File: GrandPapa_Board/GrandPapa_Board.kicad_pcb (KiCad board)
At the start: 4 copper layers, 82 x 82 mm, 98 parts, among them J1 3.7V LiPo Single Cell, J11 Dupont 01x04_Male, J2 HARWIN_ROCKET, J3 Dupont_GPS, J4 HARWIN_MINISENSOR, J5 Dupont_Logger, J6 PROG Header, J7 HARWIN_KALMAN, J8 Therm EN Jumper, U1 MCP1642B-50I/MS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

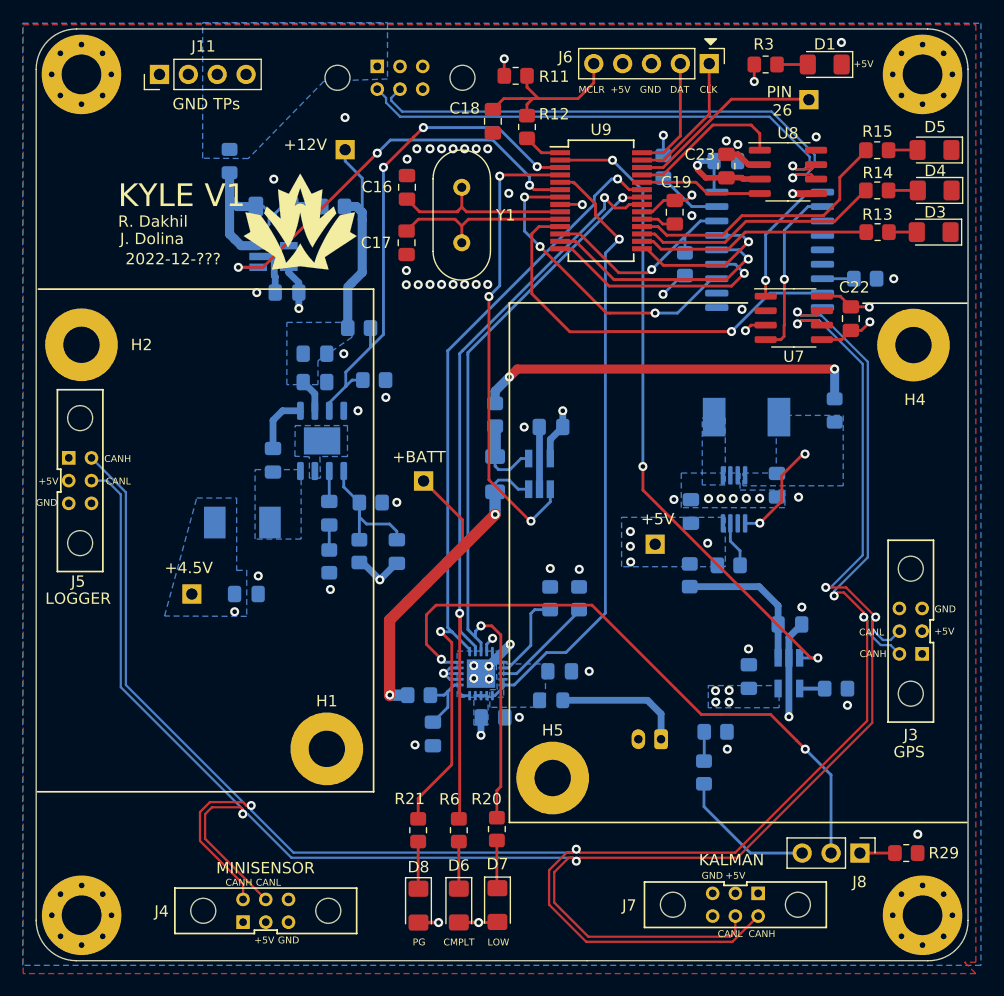
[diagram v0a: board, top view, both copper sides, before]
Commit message: Address Jack's comments, minor schematic text cleanup
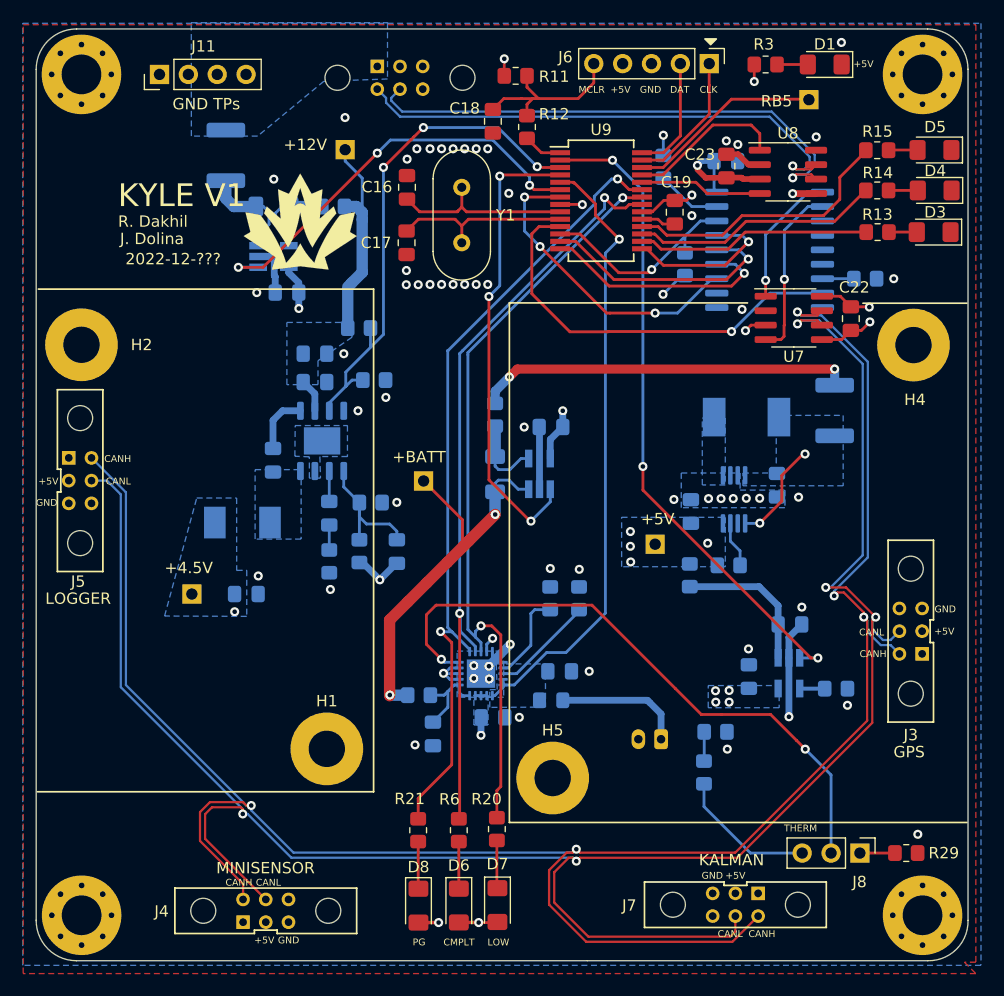
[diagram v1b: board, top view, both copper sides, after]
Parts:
- F1: footprint Fuse:Fuse_0805_2012Metric_Pad1.15x1.40mm_HandSolder -> Fuse:Fuse_1812_4532Metric_Pad1.30x3.40mm_HandSolder
- F2: value 1.2A -> 1.5A; footprint Fuse:Fuse_0805_2012Metric_Pad1.15x1.40mm_HandSolder -> Fuse:Fuse_1812_4532Metric_Pad1.30x3.40mm_HandSolder
- R29: value 15kR -> 10kR
- R4: value 2kR -> 10kR
- moved F1 0.60 mm to (130.0, 71.4)
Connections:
- net /Battery Charging/BATT_CHARGER_PG renamed /Battery Charging/BATT_CHARGER_PG_L
- net /Battery Charging/BATT_CHARGE_COMPLETE renamed /Battery Charging/BATT_CHARGE_COMPLETE_L
- net /Battery Charging/LOW_BAT renamed /Battery Charging/LOW_BAT_L
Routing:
- net Net-(F1-Pad2): track 15.6 -> 9.21 mm
- net +BATT: track 34.4 -> 33.2 mm
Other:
- board text added: "RB5"
- board text added: "THERM"
- board text removed: "PIN 26"

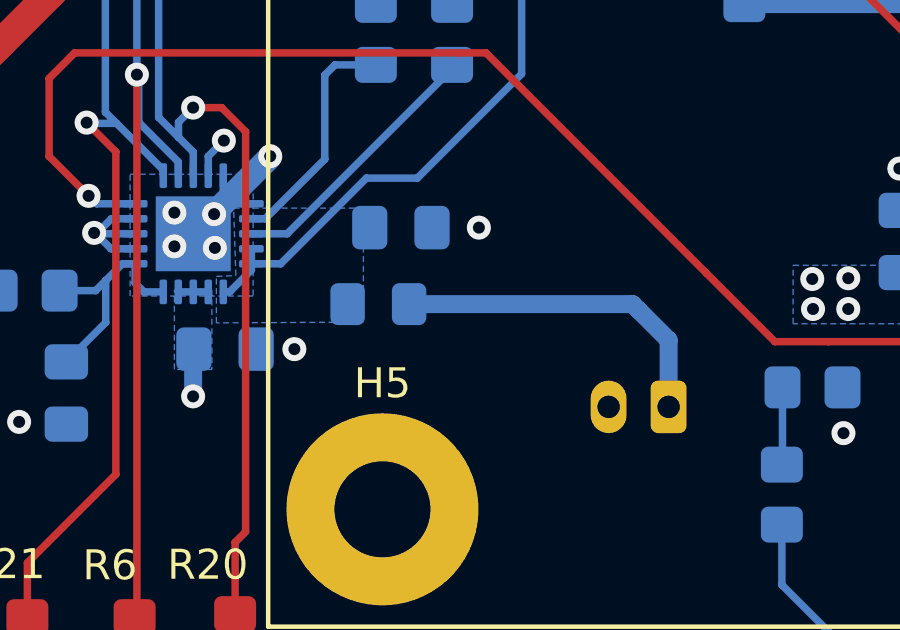
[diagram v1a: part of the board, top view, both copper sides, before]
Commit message: missed F3, update PDF
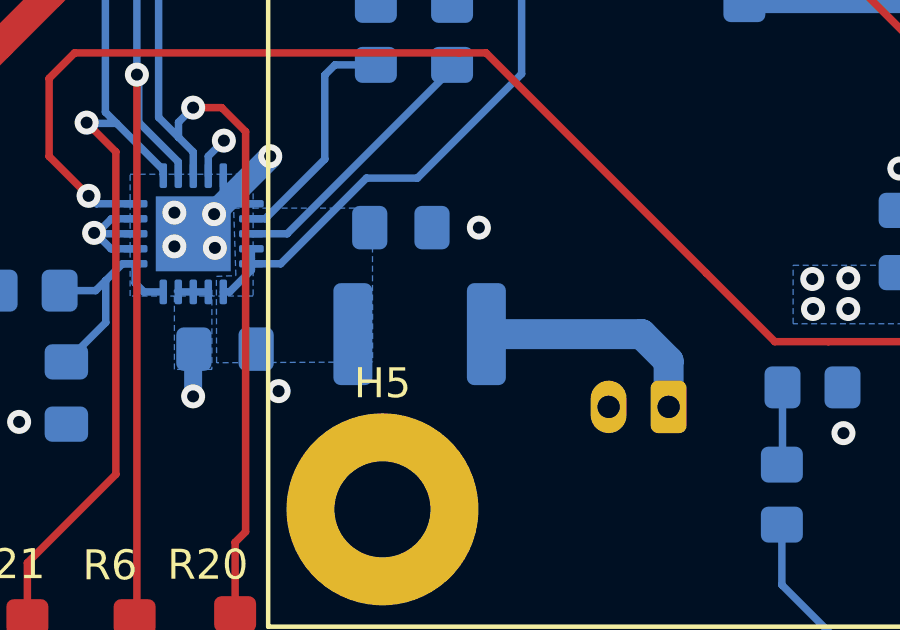
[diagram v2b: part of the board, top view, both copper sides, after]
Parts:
- F3: footprint Fuse:Fuse_0805_2012Metric_Pad1.15x1.40mm_HandSolder -> Fuse:Fuse_1812_4532Metric_Pad1.30x3.40mm_HandSolder
- moved F3 1.70 mm to (160.0, 120.3)
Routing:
- net Net-(F3-Pad1): track 11.4 -> 7.97 mm
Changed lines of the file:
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@@
     )
   )
-  (footprint "Fuse:Fuse_0805_2012Metric_Pad1.15x1.40mm_HandSolder" (layer "B.Cu")
-    (at 158.614 119.3218 180)
-    (descr "Fuse SMD 0805 (2012 Metric), square (rectangular) end terminal, IPC_7351 nominal with elongated pad for handsoldering. (Body size source: https://docs.google.com/spreadsheets/d/1BsfQQcO9C6DZCsRaXUlFlo91Tg2WpOkGARC1WS5S8t0/edit?usp=sharing), generated with kicad-footprint-generator")
+  (footprint "Fuse:Fuse_1812_4532Metric_Pad1.30x3.40mm_HandSolder" (layer "B.Cu")
+    (at 159.989 120.3218 180)
+    (descr "Fuse SMD 1812 (4532 Metric), square (rectangular) end terminal, IPC_7351 nominal with elongated pad for handsoldering. (Body size source: https://www.nikhef.nl/pub/departments/mt/projects/detectorR_D/dtddice/ERJ2G.pdf), generated with kicad-footprint-generator")
     (tags "fuse handsolder")
     (property "Sheetfile" "grandpapa_Charge.kicad_sch")
     (property "Sheetname" "Battery Charging")
     (attr smd)
-    (fp_text reference "F3" (at 0 -1.905) (layer "B.SilkS")
-      (effects (font (size 1 1) (thickness 0.15)) (justify mirror))
-    )
-    (fp_text value "1.5A" (at 0 -1.65) (layer "B.Fab")
+    (fp_text reference "F3" (at -3.95 0) (layer "B.SilkS")
+      (effects (font (size 1 1) (thickness 0.15)) (justify mirror))
+    )
+    (fp_text value "1.5A" (at 0 -2.65) (layer "B.Fab")
       (effects (font (size 1 1) (thickness 0.15)) (justify mirror))
     )
     (fp_text user "${REFERENCE}" (at 0 0) (layer "B.Fab")
-      (effects (font (size 0.5 0.5) (thickness 0.08)) (justify mirror))
-    )
-    (fp_line (start -0.261252 0.71) (end 0.261252 0.71) (layer "B.SilkS") (width 0.12))
-    (fp_line (start -0.261252 -0.71) (end 0.261252 -0.71) (layer "B.SilkS") (width 0.12))
-    (fp_line (start -1.85 0.95) (end 1.85 0.95) (layer "B.CrtYd") (width 0.05))
-    (fp_line (start 1.85 0.95) (end 1.85 -0.95) (layer "B.CrtYd") (width 0.05))
-    (fp_line (start 1.85 -0.95) (end -1.85 -0.95) (layer "B.CrtYd") (width 0.05))
-    (fp_line (start -1.85 -0.95) (end -1.85 0.95) (layer "B.CrtYd") (width 0.05))
-    (fp_line (start -1 -0.6) (end -1 0.6) (layer "B.Fab") (width 0.1))
-    (fp_line (start 1 -0.6) (end -1 -0.6) (layer "B.Fab") (width 0.1))
-    (fp_line (start 1 0.6) (end 1 -0.6) (layer "B.Fab") (width 0.1))
-    (fp_line (start -1 0.6) (end 1 0.6) (layer "B.Fab") (width 0.1))
-    (pad "1" smd roundrect (at -1.025 0 180) (size 1.15 1.4) (layers "B.Cu" "B.Paste" "B.Mask") (roundrect_rratio 0.217391)
+      (effects (font (size 1 1) (thickness 0.15)) (justify mirror))
+    )
+    (fp_line (start -1.386252 1.71) (end 1.386252 1.71) (layer "B.SilkS") (width 0.12))
+    (fp_line (start -1.386252 -1.71) (end 1.386252 -1.71) (layer "B.SilkS") (width 0.12))
+    (fp_line (start 3.12 -1.95) (end -3.12 -1.95) (layer "B.CrtYd") (width 0.05))
+    (fp_line (start 3.12 1.95) (end 3.12 -1.95) (layer "B.CrtYd") (width 0.05))
+    (fp_line (start -3.12 1.95) (end 3.12 1.95) (layer "B.CrtYd") (width 0.05))
+    (fp_line (start -3.12 -1.95) (end -3.12 1.95) (layer "B.CrtYd") (width 0.05))
+    (fp_line (start 2.25 1.6) (end 2.25 -1.6) (layer "B.Fab") (width 0.1))
+    (fp_line (start -2.25 1.6) (end 2.25 1.6) (layer "B.Fab") (width 0.1))
+    (fp_line (start 2.25 -1.6) (end -2.25 -1.6) (layer "B.Fab") (width 0.1))
+    (fp_line (start -2.25 -1.6) (end -2.25 1.6) (layer "B.Fab") (width 0.1))
+    (pad "1" smd roundrect (at -2.225 0 180) (size 1.3 3.4) (layers "B.Cu" "B.Paste" "B.Mask") (roundrect_rratio 0.192308)
       (net 28 "Net-(F3-Pad1)") (pintype "passive"))
-    (pad "2" smd roundrect (at 1.025 0 180) (size 1.15 1.4) (layers "B.Cu" "B.Paste" "B.Mask") (roundrect_rratio 0.217391)
+    (pad "2" smd roundrect (at 2.225 0 180) (size 1.3 3.4) (layers "B.Cu" "B.Paste" "B.Mask") (roundrect_rratio 0.192308)
       (net 13 "/Battery Charging/VBATT_VOLT_SENSE") (pintype "passive"))
-    (model "${KICAD6_3DMODEL_DIR}/Fuse.3dshapes/Fuse_0805_2012Metric.wrl"
+    (model "${KICAD6_3DMODEL_DIR}/Fuse.3dshapes/Fuse_1812_4532Metric.wrl"
       (offset (xyz 0 0 0))
       (scale (xyz 1 1 1))
@@
   (via (at 145.034 101.9048) (size 0.8) (drill 0.4) (layers "F.Cu" "B.Cu") (free) (net 2))
   (via (at 151.814 117.3968) (size 0.8) (drill 0.4) (layers "F.Cu" "B.Cu") (net 2))
-  (via (at 155.814 120.8218) (size 0.8) (drill 0.4) (layers "F.Cu" "B.Cu") (free) (net 2))
+  (via (at 155.289 122.2218) (size 0.8) (drill 0.4) (layers "F.Cu" "B.Cu") (free) (net 2))
   (via (at 156.241539 95.278234) (size 0.8) (drill 0.4) (layers "F.Cu" "B.Cu") (free) (net 2))
   (via (at 144.0685 92.669) (size 0.8) (drill 0.4) (layers "F.Cu" "B.Cu") (free) (net 2))
@@
   (segment (start 183.564 90.1768) (end 183.559 90.1718) (width 0.25) (layer "B.Cu") (net 27))
   (segment (start 153.689 92.1218) (end 153.689 93.1968) (width 0.8) (layer "B.Cu") (net 27))
-  (segment (start 167.289 119.5218) (end 167.089 119.3218) (width 0.6) (layer "B.Cu") (net 28))
-  (segment (start 168.289 120.5218) (end 168.289 122.7468) (width 0.6) (layer "B.Cu") (net 28))
-  (segment (start 167.089 119.3218) (end 159.639 119.3218) (width 0.6) (layer "B.Cu") (net 28))
-  (segment (start 167.289 119.5218) (end 168.289 120.5218) (width 0.6) (layer "B.Cu") (net 28))
+  (segment (start 168.289 121.2218) (end 168.289 122.7468) (width 1) (layer "B.Cu") (net 28))
+  (segment (start 167.389 120.3218) (end 168.289 121.2218) (width 1) (layer "B.Cu") (net 28))
+  (segment (start 162.214 120.3218) (end 167.389 120.3218) (width 1) (layer "B.Cu") (net 28))
   (segment (start 172.526 63.2968) (end 172.526 65.1968) (width 0.25) (layer "F.Cu") (net 29))
   (segment (start 172.526 65.1968) (end 172.531 65.2018) (width 0.25) (layer "F.Cu") (net 29))
@@
     (polygon
       (pts
-        (xy 158.114 119.9218)
-        (xy 153.214 119.9468)
+        (xy 158.422034 121.250207)
+        (xy 153.22078 121.275605)
         (xy 153.214 118.3968)
         (xy 153.864 118.3718)
         (xy 153.789 116.1218)
-        (xy 158.114 116.1218)
+        (xy 158.415254 116.121402)
       )
     )

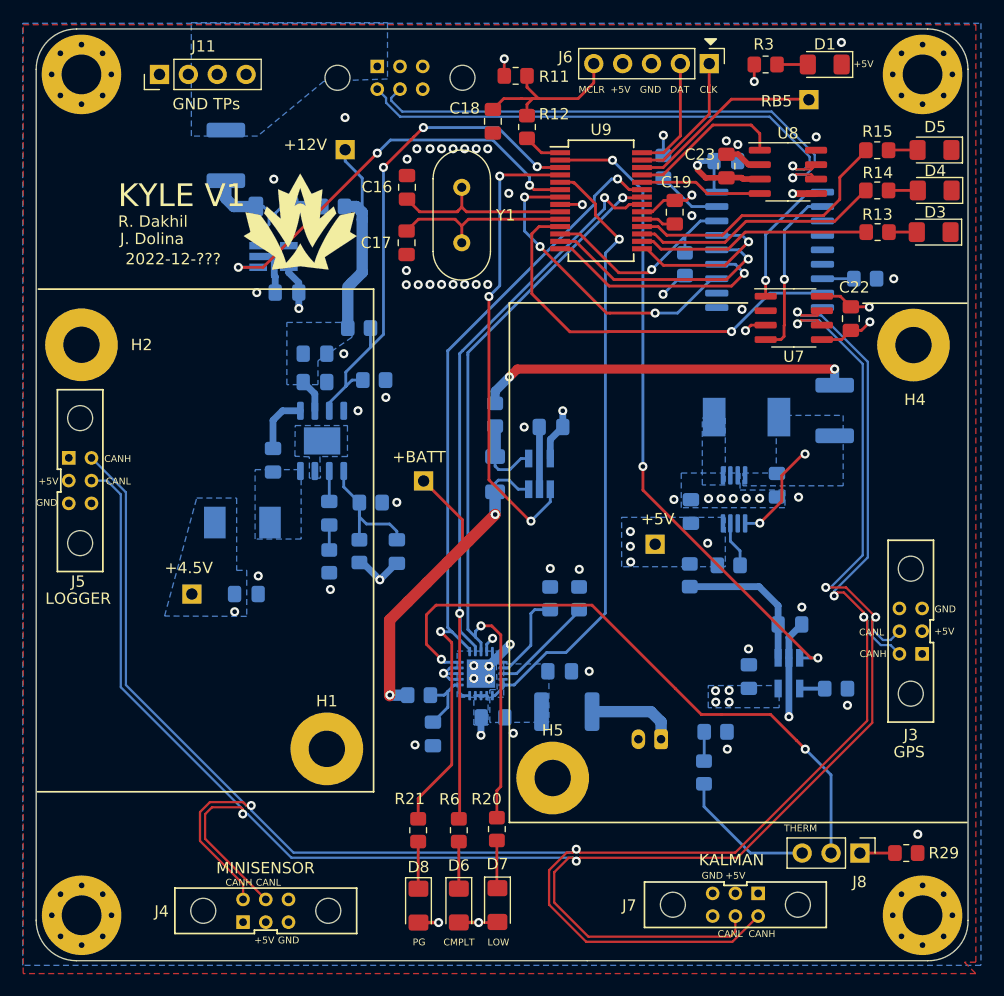
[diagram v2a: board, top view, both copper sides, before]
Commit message: Move/rotate Harwins
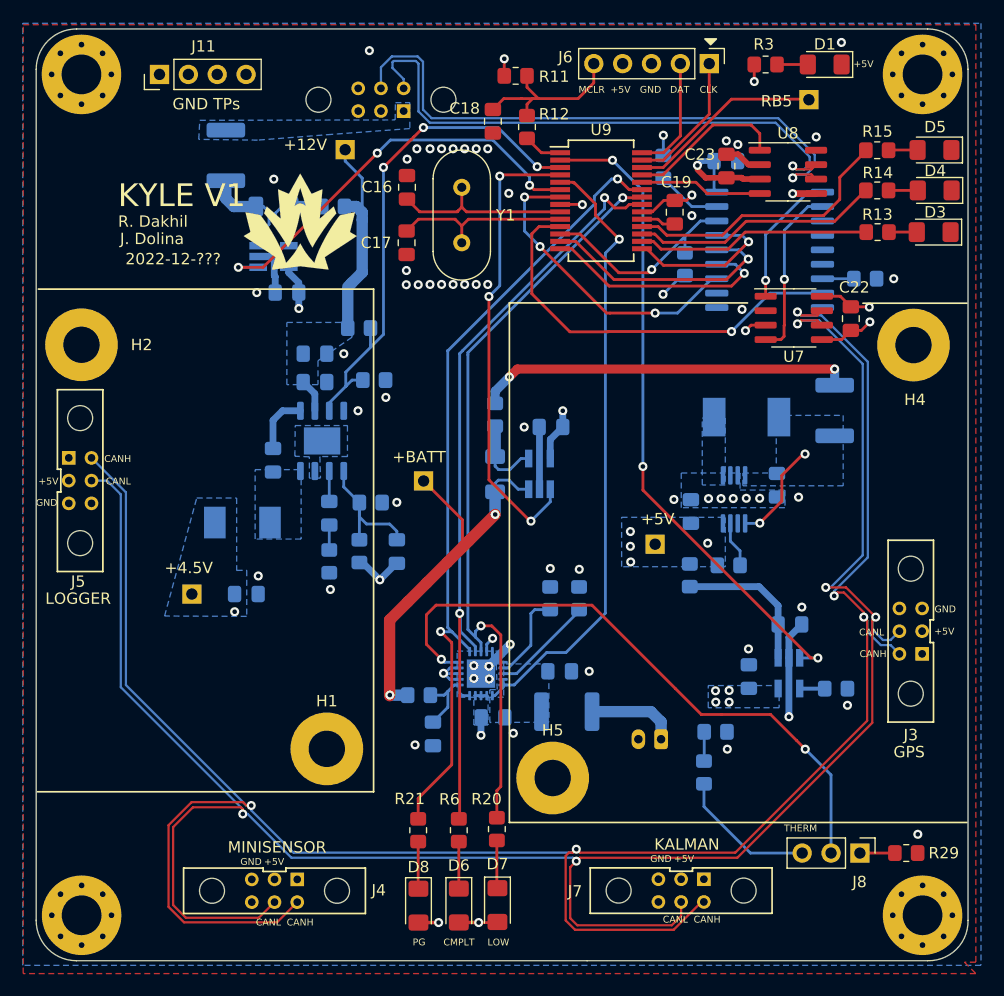
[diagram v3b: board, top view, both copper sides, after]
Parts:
- moved J7 4.93 mm to (170.1, 136.1)
- moved J2 2.56 mm to (143.6, 66.5), turned to 180 degrees
- moved J4 1.92 mm to (134.3, 136.1), turned to 180 degrees
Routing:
- net /CANH_PAYLOAD: track 189.4 -> 196.7 mm
- net /MCU and CAN Controllers/CANL_ROCKET: track 46.3 -> 52.2 mm
- net /MCU and CAN Controllers/CANH_ROCKET: track 45.5 -> 50.2 mm
- net /CANL_PAYLOAD: track 185.9 -> 189.2 mm

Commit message: route CAN diff pairs, generate gerbers
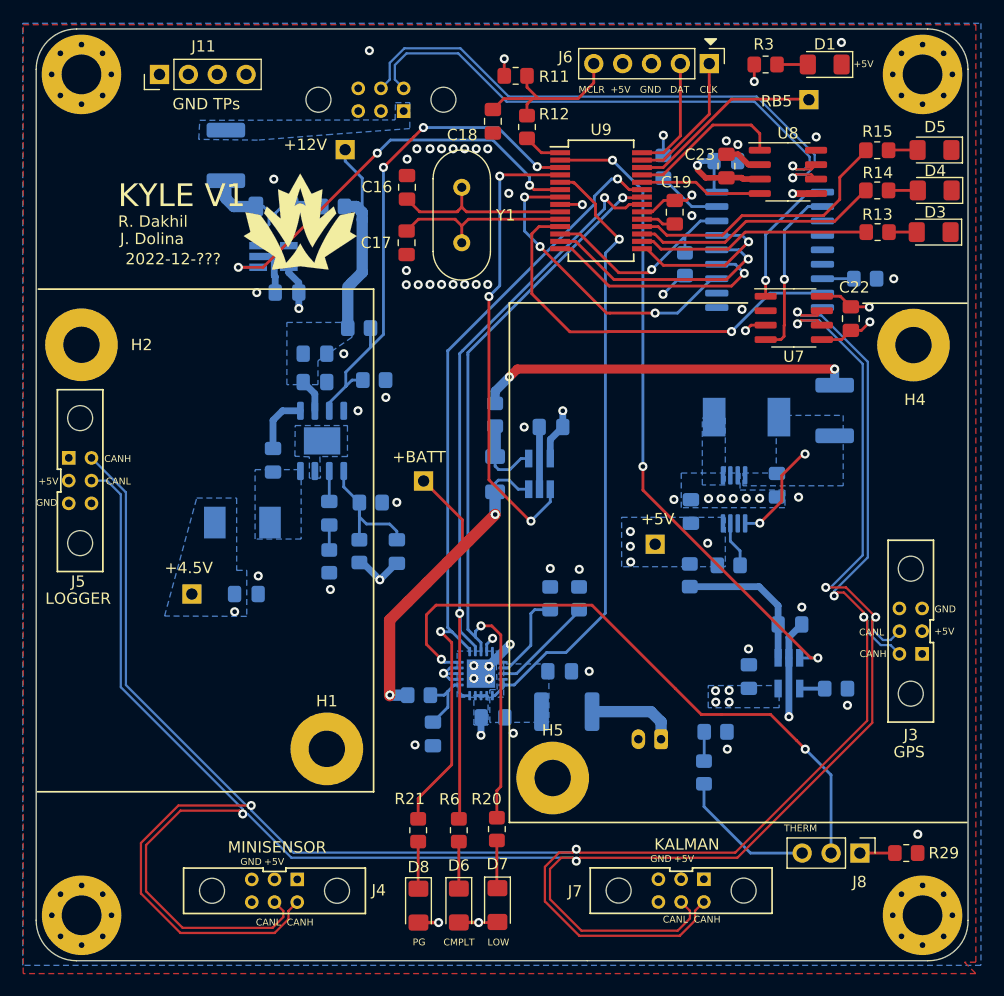
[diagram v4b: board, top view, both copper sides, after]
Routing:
- net /CANL_PAYLOAD: track 189.2 -> 198.8 mm
- net /CANH_PAYLOAD: track 196.7 -> 204.0 mm
- net /MCU and CAN Controllers/CANH_ROCKET: track 50.2 -> 47.8 mm
- net /MCU and CAN Controllers/CANL_ROCKET: track 52.2 -> 50.1 mm
